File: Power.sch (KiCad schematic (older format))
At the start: 0 parts

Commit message: Power Filtering & Protection Module
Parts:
- added C? (x2): C, ~, symbol C
- added F? (x4): FUSE, ~, symbol FUSE
- added L? (x2): INDUCTOR, ~, symbol INDUCTOR
- added P?: ATX-PWR, ~, symbol ATX-PWR
- added R?: R, ~, symbol R
- added SW?: SPST, ~, symbol SPST
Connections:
- new net: F?.2, P?.1 (3v3-1), P?.2 (3v3-2)
- new net: F?.2, P?.10 (12v-1)
- new net: F?.1, P?.14 (-12v)
- new net: P?.16 (Pwr-On), R?.1, SW?.1
- new net: F?.2, P?.4 (5v-1), P?.6 (5v-2)
- new net +12P: F?.1, L?.1
- new net +12V: C?.1, L?.2
- new net +3.3V: F?.1, R?.2
- new net +5V: F?.1
- new net -12P: F?.2, L?.1
- new net -12V: C?.2, L?.2
- new net GND: C?.1, C?.2, P?.3 (GND-1), P?.5 (GND-2), SW?.2

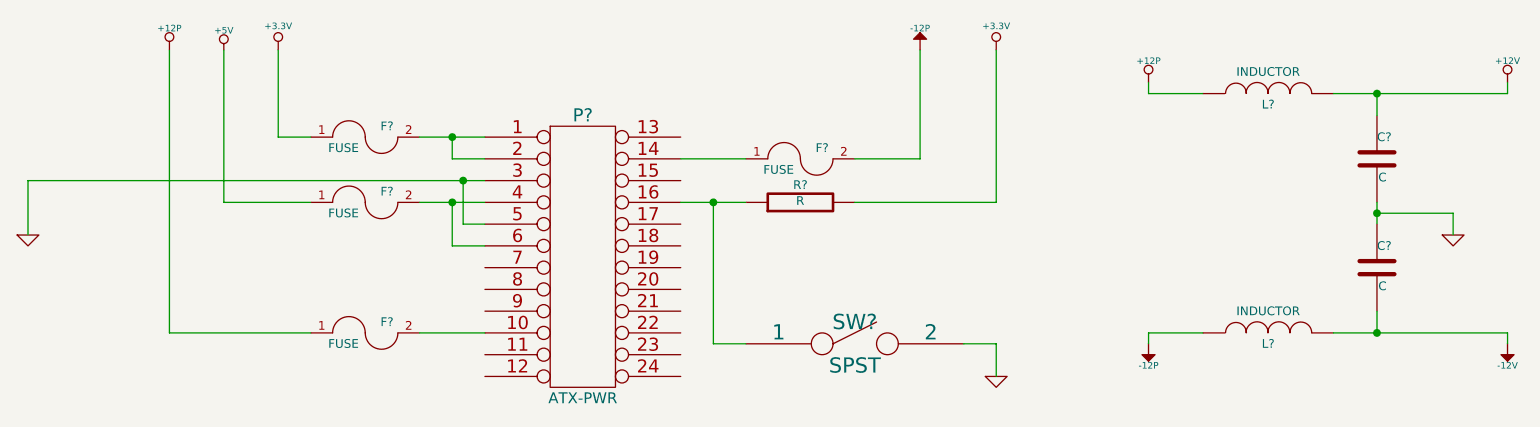
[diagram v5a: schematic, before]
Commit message: Fan/Current Module Refactor
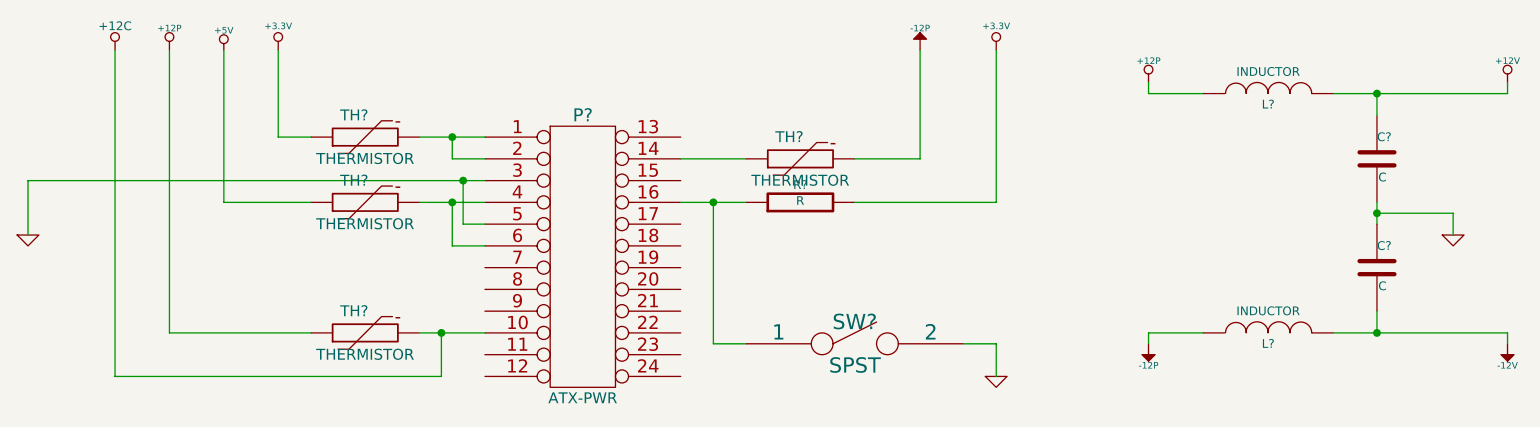
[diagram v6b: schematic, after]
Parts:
- removed F? (x4): FUSE, ~, symbol FUSE
- added TH? (x4): THERMISTOR, ~, symbol THERMISTOR
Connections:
- net +12P: now also TH?.1
- net +3.3V: now also TH?.1
- net +5V: now also TH?.1
- net -12P: now also TH?.2
- net at P?.1 (3v3-1), P?.2 (3v3-2): now also TH?.2
- net +12C: now reaches P?.10 (12v-1)
- net +12C: now also TH?.2
- net at P?.14 (-12v): now also TH?.1
- net at P?.4 (5v-1), P?.6 (5v-2): now also TH?.2
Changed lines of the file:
@@
 Sheet 4 9
 Title ""
-Date "22 oct 2013"
+Date "23 oct 2013"
 Rev ""
 Comp ""
@@
 F 3 "~" H 1700 1100 60  0000 C CNN
 	1    1700 1100
-	1    0    0    -1
-$EndComp
-$Comp
-L FUSE F?
-U 1 1 524E4F1E
-P 2350 1500
-F 0 "F?" H 2450 1550 40  0000 C CNN
-F 1 "FUSE" H 2250 1450 40  0000 C CNN
-F 2 "~" H 2350 1500 60  0000 C CNN
-F 3 "~" H 2350 1500 60  0000 C CNN
-	1    2350 1500
-	1    0    0    -1
-$EndComp
-$Comp
-L FUSE F?
-U 1 1 524E4F35
-P 2350 1800
-F 0 "F?" H 2450 1850 40  0000 C CNN
-F 1 "FUSE" H 2250 1750 40  0000 C CNN
-F 2 "~" H 2350 1800 60  0000 C CNN
-F 3 "~" H 2350 1800 60  0000 C CNN
-	1    2350 1800
-	1    0    0    -1
-$EndComp
-$Comp
-L FUSE F?
-U 1 1 524E4F3B
-P 2350 2400
-F 0 "F?" H 2450 2450 40  0000 C CNN
-F 1 "FUSE" H 2250 2350 40  0000 C CNN
-F 2 "~" H 2350 2400 60  0000 C CNN
-F 3 "~" H 2350 2400 60  0000 C CNN
-	1    2350 2400
-	1    0    0    -1
-$EndComp
-$Comp
-L FUSE F?
-U 1 1 524E4F41
-P 4350 1600
-F 0 "F?" H 4450 1650 40  0000 C CNN
-F 1 "FUSE" H 4250 1550 40  0000 C CNN
-F 2 "~" H 4350 1600 60  0000 C CNN
-F 3 "~" H 4350 1600 60  0000 C CNN
-	1    4350 1600
 	1    0    0    -1
 $EndComp
@@
 	7600 1300 7600 1250
 Connection ~ 7000 1300
+$Comp
+L +12C #PWR?
+U 1 1 526C5382
+P 1200 1100
+F 0 "#PWR?" H 1200 1070 30  0001 C CNN
+F 1 "+12C" H 1200 1210 40  0000 C CNN
+F 2 "~" H 1200 1100 60  0000 C CNN
+F 3 "~" H 1200 1100 60  0000 C CNN
+	1    1200 1100
+	1    0    0    -1
+$EndComp
+Wire Wire Line
+	1200 1100 1200 2600
+Wire Wire Line
+	1200 2600 2700 2600
+Wire Wire Line
+	2700 2600 2700 2400
+Connection ~ 2700 2400
+$Comp
+L THERMISTOR TH?
+U 1 1 526C569C
+P 4350 1600
+F 0 "TH?" V 4450 1650 50  0000 C CNN
+F 1 "THERMISTOR" V 4250 1600 50  0000 C CNN
+F 2 "~" H 4350 1600 60  0000 C CNN
+F 3 "~" H 4350 1600 60  0000 C CNN
+	1    4350 1600
+	0    -1   -1   0
+$EndComp
+$Comp
+L THERMISTOR TH?
+U 1 1 526C56A9
+P 2350 1500
+F 0 "TH?" V 2450 1550 50  0000 C CNN
+F 1 "THERMISTOR" V 2250 1500 50  0000 C CNN
+F 2 "~" H 2350 1500 60  0000 C CNN
+F 3 "~" H 2350 1500 60  0000 C CNN
+	1    2350 1500
+	0    -1   -1   0
+$EndComp
+$Comp
+L THERMISTOR TH?
+U 1 1 526C56AF
+P 2350 1800
+F 0 "TH?" V 2450 1850 50  0000 C CNN
+F 1 "THERMISTOR" V 2250 1800 50  0000 C CNN
+F 2 "~" H 2350 1800 60  0000 C CNN
+F 3 "~" H 2350 1800 60  0000 C CNN
+	1    2350 1800
+	0    -1   -1   0
+$EndComp
+$Comp
+L THERMISTOR TH?
+U 1 1 526C56B5
+P 2350 2400
+F 0 "TH?" V 2450 2450 50  0000 C CNN
+F 1 "THERMISTOR" V 2250 2400 50  0000 C CNN
+F 2 "~" H 2350 2400 60  0000 C CNN
+F 3 "~" H 2350 2400 60  0000 C CNN
+	1    2350 2400
+	0    -1   -1   0
+$EndComp
 $EndSCHEMATC
